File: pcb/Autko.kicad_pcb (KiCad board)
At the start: 4 copper layers, 140 x 155 mm, 121 parts, among them J1 PDI, M1 LEFT, M2 RIGHT, Q1 Si4368DY, SW1 POWER, SW2 START, SW3 STOP, U1 LTC3872, U10 CNY70, U11 CNY70, U12 TB6612FNG, U13 74HC14, U14 RN4678, U2 TLV1117-33, U3 ATxmega16A4U-A, U5 CNY70, U6 CNY70, U7 CNY70, U8 CNY70, U9 CNY70, Y1 8MHz

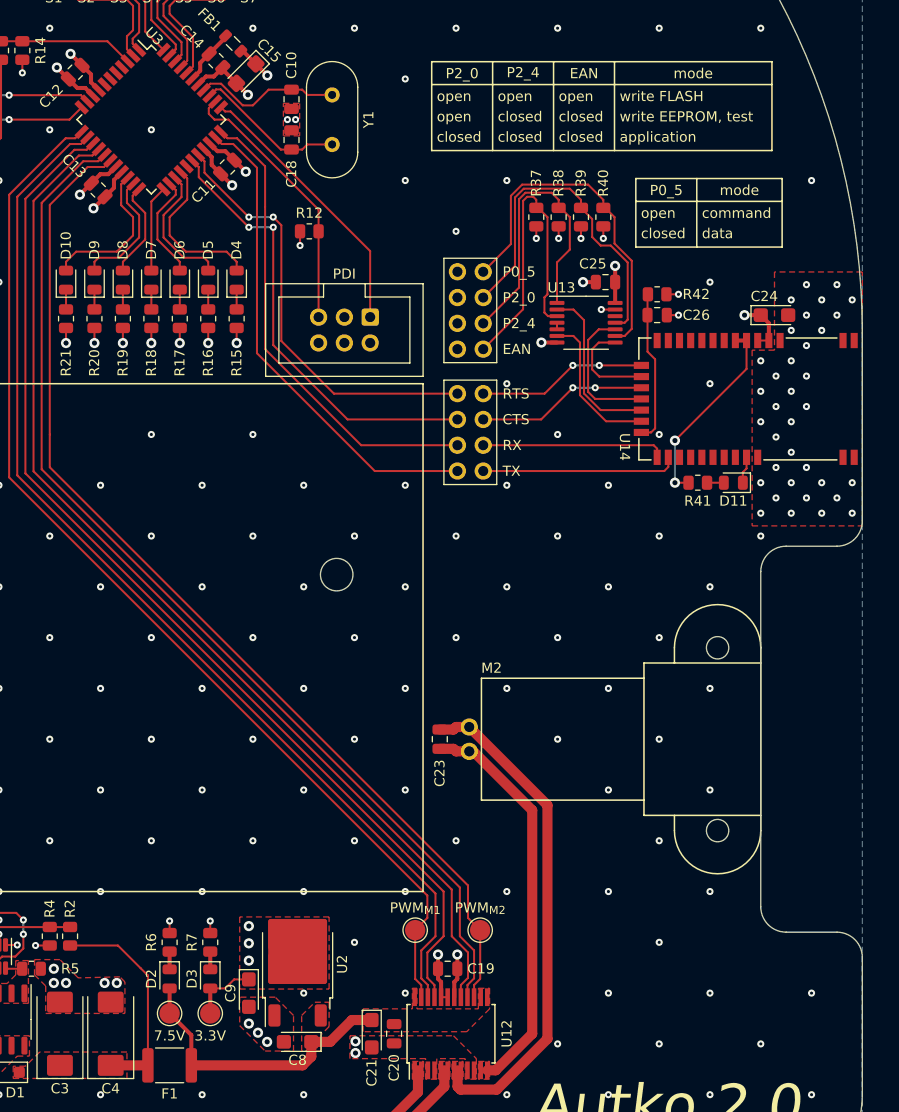
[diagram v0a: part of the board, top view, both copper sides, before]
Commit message: [pcb] BT config rework
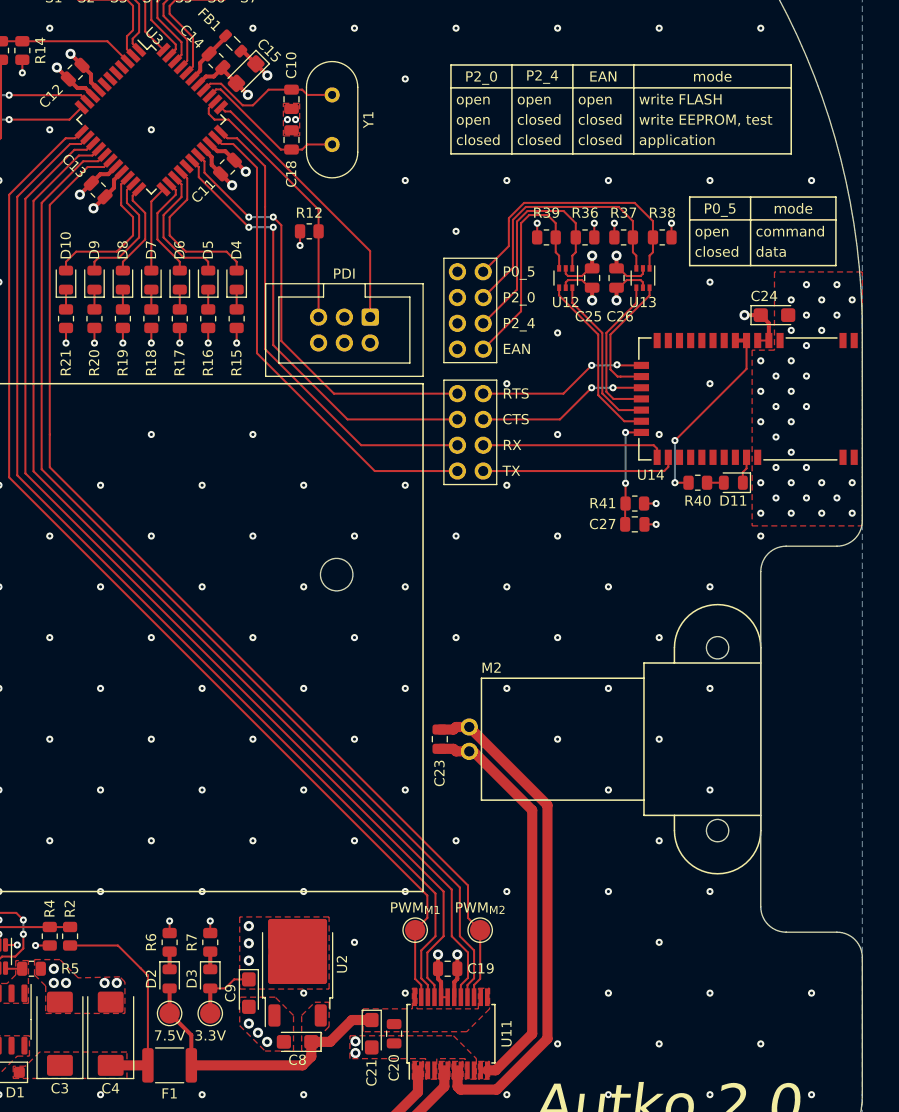
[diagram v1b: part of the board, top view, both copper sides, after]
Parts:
- added C26: 100nF, Capacitor_SMD:C_0805_2012Metric, F.Cu at (145.3, 95.1)
- added U12: 74HC2G14, Package_TO_SOT_SMD:SOT-363_SC-70-6, F.Cu at (140.3, 95.1)
- D10, D4, D5, D6, D7, D8, D9: value YELLOW -> ORANGE
- R15, R16, R17, R18, R19, R20, R21: value ???R -> 680R
- R6: value ?R -> 5.1kR
- R7: value ?R -> 820kR
- U13: value 74HC14 -> 74HC2G14; footprint Package_SO:TSSOP-14_4.4x5mm_P0.65mm -> Package_TO_SOT_SMD:SOT-363_SC-70-6
- moved C27 20.7 mm to (147.1, 119.3)
- moved R41 20.7 mm to (147.1, 117.3)
- moved U13 7.12 mm to (147.9, 95.1), turned to -90 degrees
- moved R38 6.14 mm to (149.8, 91.1), turned to 180 degrees
- moved R37 4.65 mm to (146.0, 91.1), turned to 0 degrees
- moved R36 3.28 mm to (142.2, 91.1), turned to 180 degrees
- moved R39 2.24 mm to (138.4, 91.1), turned to 180 degrees
- moved C25 1.37 mm to (142.9, 95.1), turned to 90 degrees
- renumbered C26 to C27, R38 to R36, R39 to R37, R40 to R38, R37 to R39, R41 to R40, R42 to R41, TP15 to TP14, TP16 to TP15, U11 to U10, U12 to U11, U5 to U4, U6 to U5, U7 to U6, U8 to U7, U9 to U8, U10 to U9
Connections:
- JP1 pad 2: GND -> +3.3V
- R39 pad 1: +3.3V -> Net-(JP1-Pad1)
- R39 pad 2: Net-(JP1-Pad1) -> GND
- U13 pad 1: Net-(JP1-Pad3) -> Net-(JP1-Pad7)
- U13 pad 2: /Bluetooth/P2_4 -> GND
- U13 pad 3: Net-(JP1-Pad1) -> Net-(JP1-Pad5)
- U13 pad 4: Net-(U13-Pad4) -> /Bluetooth/P2_0
- U13 pad 5: Net-(U13-Pad4) -> +3.3V
- U13 pad 6: /Bluetooth/EAN -> /Bluetooth/P0_5
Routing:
- net Net-(JP1-Pad1): track 31.0 -> 22.6 mm
- net Net-(JP1-Pad7): track 34.7 -> 26.5 mm
- net Net-(JP1-Pad5): track 34.1 -> 26.4 mm
- net GND: track 60.9 -> 67.7 mm, vias 308 -> 309
- net Net-(JP1-Pad3): track 29.4 -> 22.7 mm
- net +3.3V: track 63.9 -> 69.3 mm
- net /Bluetooth/~{RST}: track 15.0 -> 10.6 mm, vias 0 -> 2
- net /Bluetooth/P0_5: track 9.67 -> 13.0 mm
- net /Bluetooth/EAN: track 14.8 -> 17.5 mm
- net /Bluetooth/P2_0: track 13.7 -> 15.2 mm
- net Net-(U13-Pad4): track 0.65 -> 0.00 mm

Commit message: [pcb] Almost ready
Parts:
- added R41: 330R, Resistor_SMD:R_0805_2012Metric, F.Cu at (142.9, 115.3)
- added R42: 330R, Resistor_SMD:R_0805_2012Metric, F.Cu at (142.9, 112.8)
- moved D11 3.18 mm to (155.9, 118.3), turned to -90 degrees
- moved R40 3.08 mm to (153.7, 118.3), turned to 90 degrees
- moved C27 1.59 mm to (145.9, 118.3), turned to -90 degrees
- moved R43 1.41 mm to (148.1, 118.3), turned to 90 degrees
- moved JP2 1.19 mm to (132.2, 115.3)
- moved J1 0.72 mm to (121.0, 98.2)
- moved JP1 0.49 mm to (132.2, 102.6)
- renumbered R41 to R43
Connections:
- JP2 pad 1: Net-(U14-UART_TX) -> Net-(JP2-Pad1)
- JP2 pad 3: Net-(U14-UART_RX) -> Net-(JP2-Pad3)
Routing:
- net Net-(U14-UART_RX): track 18.1 -> 5.49 mm
- net Net-(U14-UART_TX): track 19.3 -> 8.37 mm
- net Net-(JP2-Pad3): track 0.00 -> 9.81 mm
- net Net-(JP2-Pad1): track 0.00 -> 9.81 mm
- net Net-(D11-K): track 2.65 -> 5.52 mm
- net /Bluetooth/P0_5: track 13.0 -> 11.9 mm, vias 0 -> 2
- net /Microcontroller/PDI_DATA: track 27.0 -> 26.3 mm
- net /Microcontroller/PDI_CLK: track 26.8 -> 26.0 mm
- net Net-(D11-A): track 1.65 -> 2.21 mm
- net /Bluetooth/EAN: track 17.5 -> 18.0 mm, vias 0 -> 2
- net Net-(U14-P0_0/RTS): track 16.9 -> 17.4 mm, vias 2 -> 0
- net Net-(U14-P1_7/CTS): track 16.8 -> 17.2 mm, vias 2 -> 0
- net /Bluetooth/P2_4: track 16.2 -> 16.4 mm, vias 0 -> 2
- net /Bluetooth/P2_0: track 15.2 -> 15.0 mm, vias 0 -> 2
- net GND: vias 309 -> 312

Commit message: [pcb] Final touches
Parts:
- moved TP4 105.2 mm to (124.5, 80.5)
- moved TP3 101.0 mm to (144.5, 160.5)
- moved TP1 24.5 mm to (44.5, 120.5)
- moved TP5 5.04 mm to (54.5, 160.5)
- moved R24 0.49 mm to (63.2, 50.8)
- moved R25 0.49 mm to (70.2, 50.8)
- moved R32 0.49 mm to (128.8, 50.8)
- moved R33 0.49 mm to (135.8, 50.8)
- moved R22 0.49 mm to (50.4, 62.0)
- moved R23 0.49 mm to (57.4, 62.0)
- moved R26 0.49 mm to (78.8, 43.5)
- moved R27 0.49 mm to (85.8, 43.5)
- moved R28 0.49 mm to (96.0, 41.0)
- moved R29 0.49 mm to (103.0, 41.0)
- moved R30 0.49 mm to (113.2, 43.5)
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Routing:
- net +BATT: track 136.1 -> 150.2 mm
- net +3.3V: track 69.3 -> 70.9 mm
- net GND: track 67.7 -> 66.4 mm, vias 312 -> 317
- net Net-(M1--): track 118.2 -> 117.1 mm
- net /Line sensors/SENSOR2: track 44.6 -> 45.4 mm
- net /Bluetooth/RTS: track 44.5 -> 43.8 mm
- net /Bluetooth/CTS: track 43.1 -> 42.4 mm
- net Net-(M2-+): track 39.9 -> 40.5 mm
- net /Microcontroller/BTN_STOP: track 46.6 -> 47.2 mm

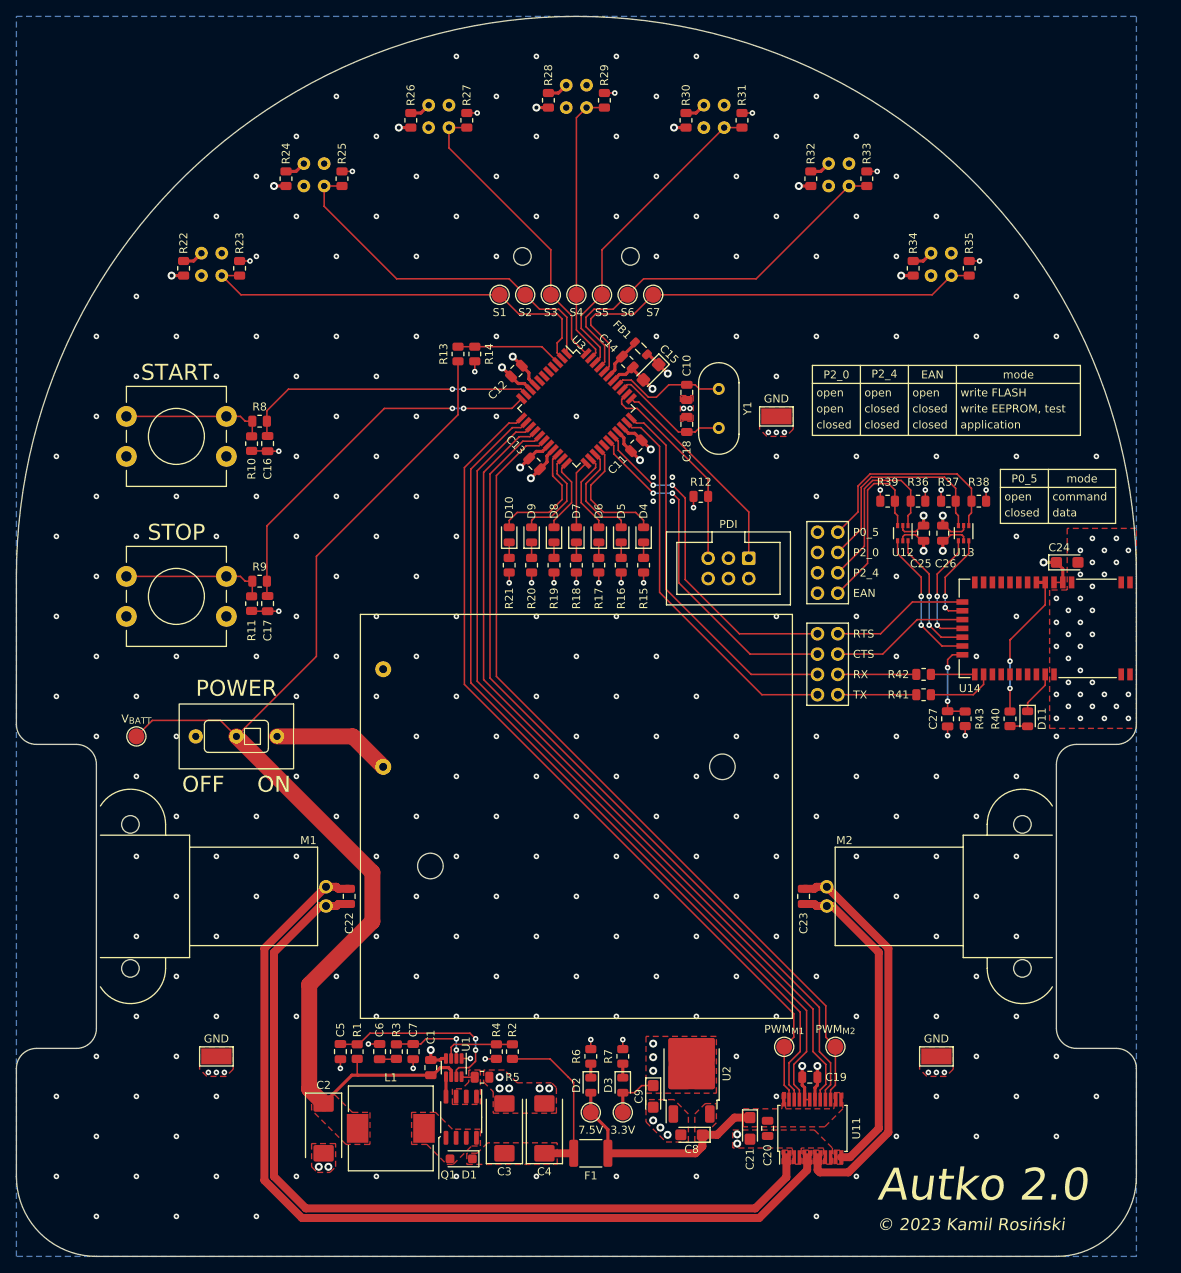
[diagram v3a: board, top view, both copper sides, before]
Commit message: [pcb] More final touches, UART test ponts added.
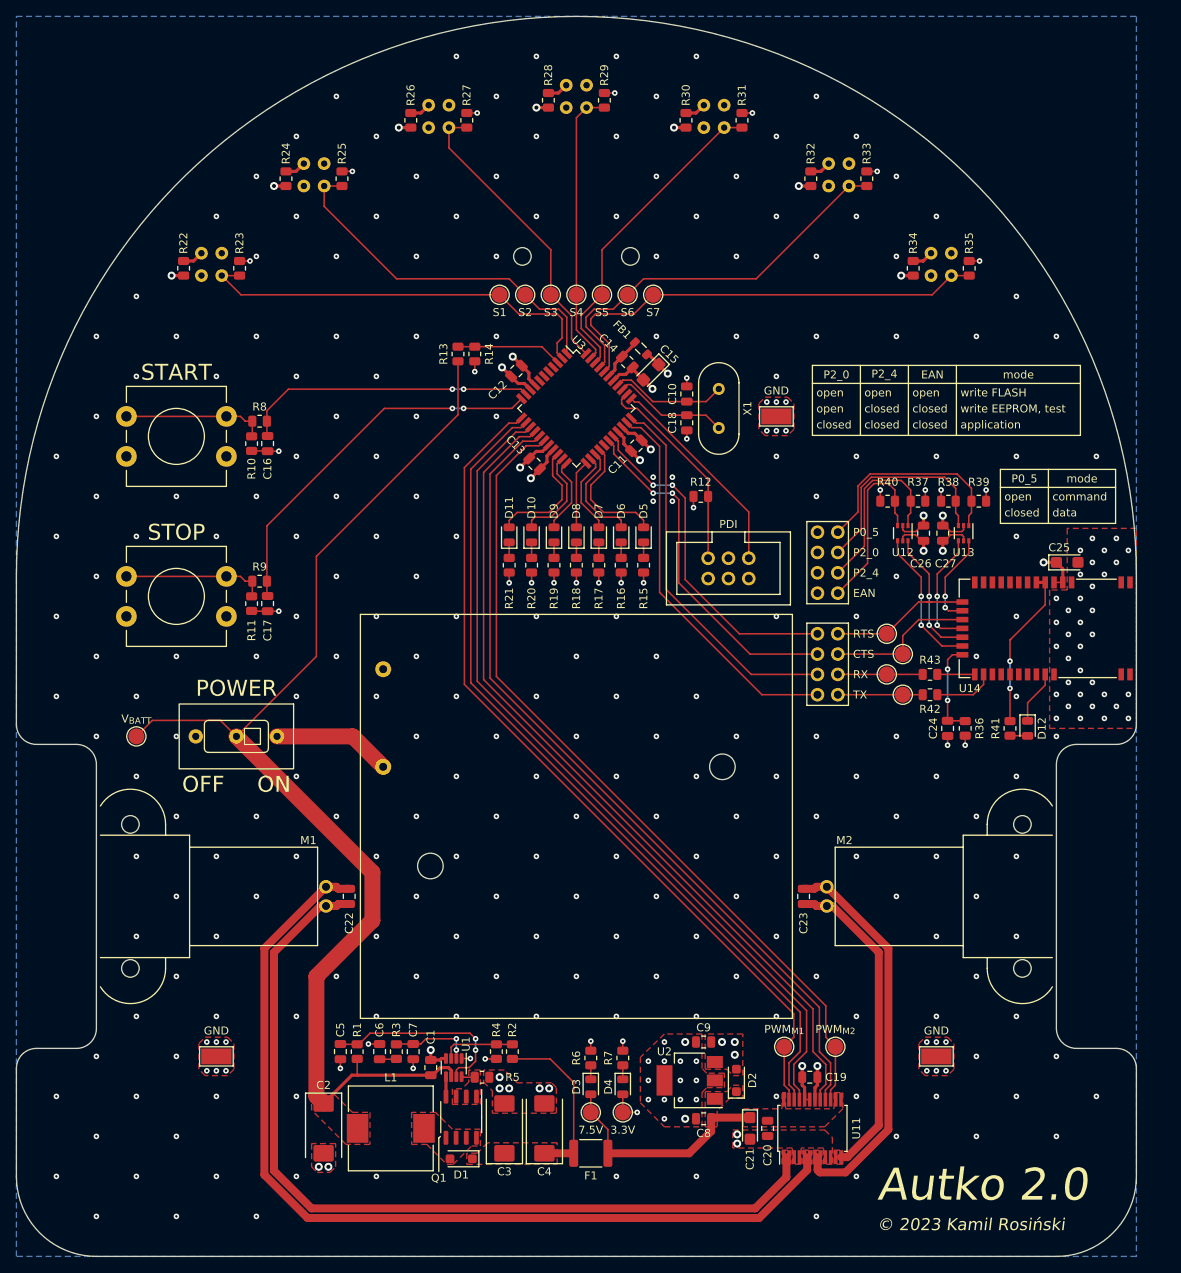
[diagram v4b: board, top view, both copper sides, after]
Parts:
- added D2: SL1A, Diode_SMD:D_SOD-123F, F.Cu at (119.5, 163.5)
- added TP16: TestPoint, TestPoint:TestPoint_Pad_D2.0mm, F.Cu at (140.3, 115.3)
- added TP17: TestPoint, TestPoint:TestPoint_Pad_D2.0mm, F.Cu at (138.3, 112.8)
- added TP18: TestPoint, TestPoint:TestPoint_Pad_D2.0mm, F.Cu at (140.3, 110.2)
- added TP19: TestPoint, TestPoint:TestPoint_Pad_D2.0mm, F.Cu at (138.3, 107.7)
- C10, C18: value 22pF -> 30pF
- C8: value 10uF -> 330nF; footprint Capacitor_Tantalum_SMD:CP_EIA-3216-18_Kemet-A -> Capacitor_SMD:C_0805_2012Metric
- C9: value 10uF -> 100nF; footprint Capacitor_Tantalum_SMD:CP_EIA-3216-18_Kemet-A -> Capacitor_SMD:C_0805_2012Metric
- FB1: value FerriteBead -> 220R
- R13: value 30kR -> 20kR
- U2: value TLV1117-33 -> uA78M33; footprint Package_TO_SOT_SMD:TO-252-2 -> Package_TO_SOT_SMD:SOT-223-3_TabPin2
- moved C9 9.27 mm to (115.4, 158.7), turned to 180 degrees
- moved C8 2.50 mm to (115.4, 168.3)
- moved C24 1.20 mm to (145.9, 119.5)
- moved D12 1.20 mm to (155.9, 119.5)
- moved R36 1.20 mm to (148.1, 119.5)
- moved R41 1.20 mm to (153.7, 119.5)
- moved U2 0.87 mm to (113.7, 163.5), turned to 180 degrees
- moved R42 0.80 mm to (143.7, 115.3)
- moved R43 0.80 mm to (143.7, 112.8)
- moved D3 0.20 mm to (101.3, 164.3)
- moved D4 0.20 mm to (105.3, 164.3)
- moved C10 0.20 mm to (113.3, 77.7), turned to 90 degrees
- moved C18 0.20 mm to (113.3, 81.3), turned to -90 degrees
- moved R6 0.20 mm to (101.3, 160.7)
- moved R7 0.20 mm to (105.3, 160.7)
- renumbered C27 to C24, C24 to C25, C25 to C26, C26 to C27, D9 to D10, D10 to D11, D11 to D12, D2 to D3, D3 to D4, D4 to D5, D5 to D6, D6 to D7, D7 to D8, D8 to D9, R43 to R36, R36 to R37, R37 to R38, R38 to R39, R39 to R40, R40 to R41, R41 to R42, R42 to R43, Y1 to X1
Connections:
- U2 pad 1: GND -> +7.5V
- U2 pad 2: +3.3V -> GND
- U2 pad 3: +7.5V -> +3.3V
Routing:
- net +3.3V: track 70.9 -> 68.3 mm, vias 30 -> 31
- net GND: track 66.4 -> 68.5 mm, vias 317 -> 337
- net Net-(U14-P0_0/RTS): track 17.4 -> 18.7 mm
- net Net-(D12-K): track 5.52 -> 6.72 mm
- net /Bluetooth/~{RST}: track 10.8 -> 12.0 mm
- net /Bluetooth/BT_3V3: track 19.1 -> 20.3 mm
- net Net-(U14-UART_TX): track 8.37 -> 7.57 mm
- net Net-(U14-UART_RX): track 5.49 -> 4.69 mm
- net Net-(JP2-Pad3): track 9.81 -> 10.6 mm
- net Net-(JP2-Pad1): track 9.81 -> 10.6 mm
- net +BATT: track 150.2 -> 149.5 mm
- net Net-(U14-P1_7/CTS): track 17.2 -> 17.8 mm

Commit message: [pcb] 10uF capacitor changed from A to T package
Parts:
- C15, C21, C25: footprint Capacitor_Tantalum_SMD:CP_EIA-3216-18_Kemet-A -> Capacitor_Tantalum_SMD:CP_EIA-3528-12_Kemet-T
- FB1: footprint Inductor_SMD:L_0805_2012Metric -> Capacitor_SMD:C_0805_2012Metric
- R13: value 20kR -> 10kR
- moved C15 0.69 mm to (109.5, 75.2)
- moved FB1 0.67 mm to (108.0, 71.5)
- moved C25 0.65 mm to (160.8, 98.1)
- moved C21 0.60 mm to (120.6, 169.5)
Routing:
- net +3.3V: track 68.3 -> 70.0 mm
- net GND: track 68.5 -> 69.5 mm, vias 337 -> 336
- net +7.5V: track 28.7 -> 27.8 mm
- net Net-(U3-AVCC): track 5.57 -> 6.36 mm

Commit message: [pcb] ERC/DRC checks
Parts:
- R7: value 820kR -> 820R
- renumbered R5 to R4, R4 to R5
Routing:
- net Net-(U14-P1_7/CTS): track 17.8 -> 17.2 mm

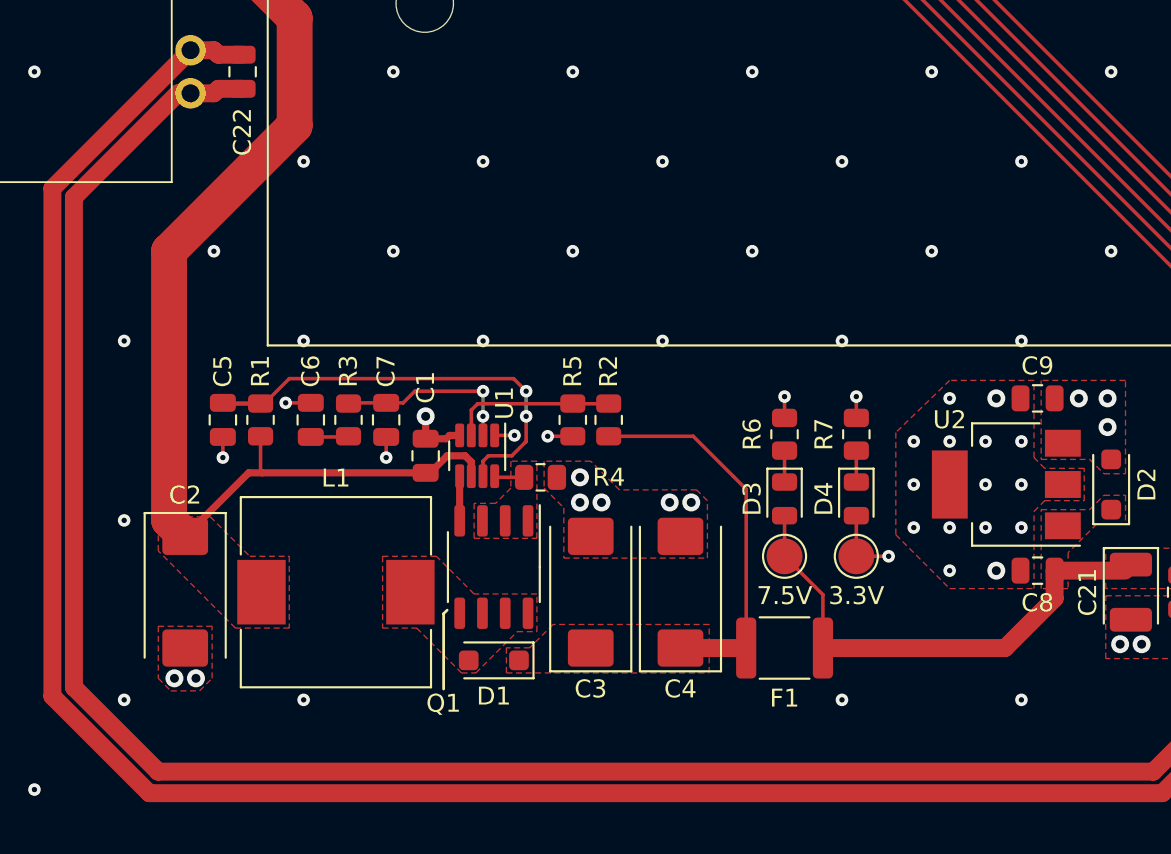
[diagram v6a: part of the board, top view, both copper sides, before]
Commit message: [pcb] Change Schottky diode
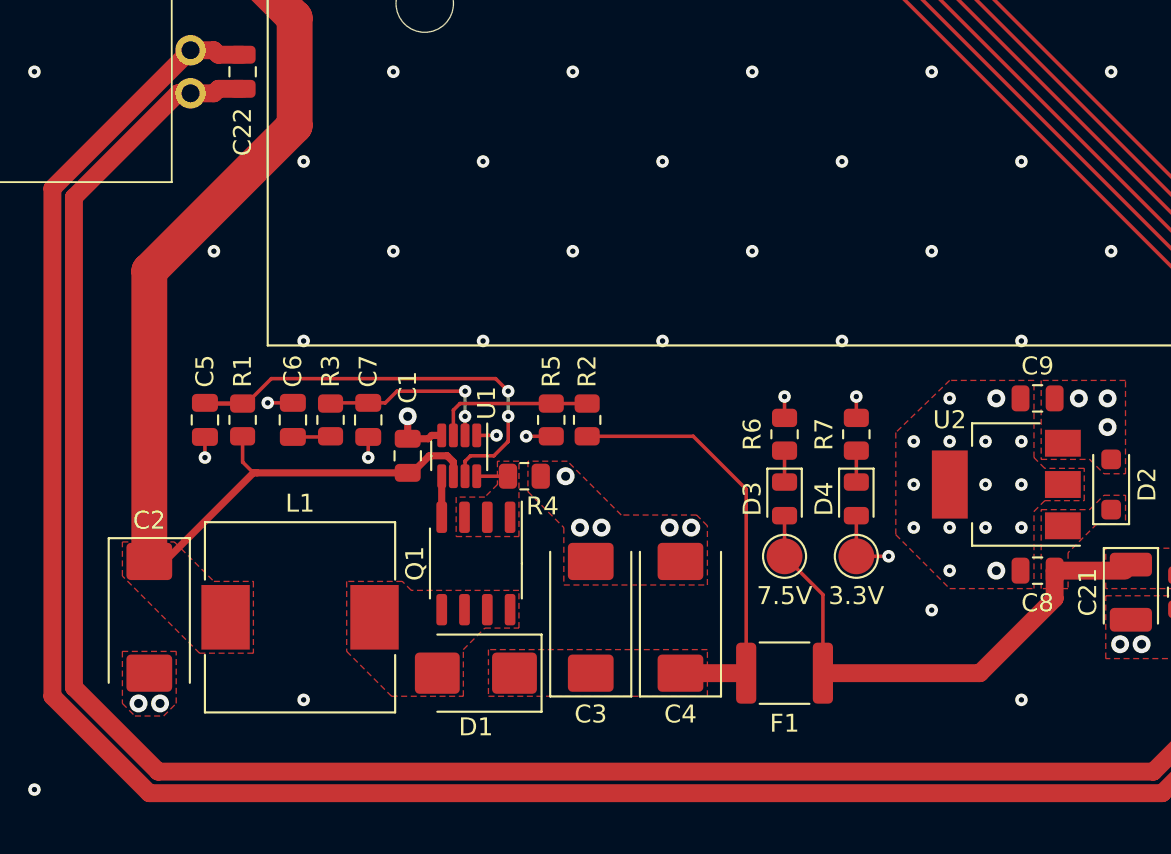
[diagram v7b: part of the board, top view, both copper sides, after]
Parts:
- D1: footprint Diode_SMD:D_SOD-123F -> Diode_SMD:D_SMB
- R2: value 10.2kR -> 53.6kR
- R5: value 53.6kR -> 10.2kR
- moved C2 2.44 mm to (65.9, 170.9)
- moved L1 2.44 mm to (74.3, 170.9)
- moved C3 1.40 mm to (90.5, 170.9)
- moved C4 1.40 mm to (95.5, 170.9)
- moved F1 1.40 mm to (101.3, 174.0)
- moved D1 1.23 mm to (84.1, 174.0)
- moved R2 1.20 mm to (90.3, 159.9)
- moved R5 1.20 mm to (88.3, 159.9)
- moved Q1 1.02 mm to (84.1, 167.9)
- moved C1 1.00 mm to (80.3, 161.9)
- moved C5 1.00 mm to (69.0, 159.9)
- moved C6 1.00 mm to (73.9, 159.9)
- moved C7 1.00 mm to (78.1, 159.9)
- moved R1 1.00 mm to (71.1, 159.9)
- moved R3 1.00 mm to (76.0, 159.9)
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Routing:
- net +BATT: track 149.5 -> 152.8 mm
- net Net-(D1-K): track 21.4 -> 24.0 mm
- net +7.5V: track 27.8 -> 29.8 mm
- net GND: vias 336 -> 333
